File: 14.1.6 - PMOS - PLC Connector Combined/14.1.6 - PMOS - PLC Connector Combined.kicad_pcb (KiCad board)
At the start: 2 copper layers, 61.5 x 67.8 mm, 114 parts, among them J201 Conn_01x01_PAD, J202 Conn_01x01_PAD, J203 Conn_01x01_PAD, J204 Conn_01x01_PAD, J205 Conn_01x01_PAD, J206 Conn_01x01_PAD, J207 Conn_01x01_PAD, J208 Conn_01x01_PAD, J209 Conn_01x01_PAD, J210 Conn_01x01_PAD, J211 Conn_01x01_PAD, J212 Conn_01x01_PAD, J213 Conn_01x01_PAD, J214 Conn_01x01_PAD, J215 Conn_01x01_PAD, J216 Conn_01x01_PAD, J217 Conn_01x01_PAD, J218 Conn_01x01_PAD, J219 Conn_01x01_PAD, J220 Conn_01x01_PAD, J221 DB128L-5.08-2P-BK-S, J222 DB128L-5.08-2P-BK-S, J223 DB128L-5.08-2P-BK-S, J224 DB128L-5.08-2P-BK-S, J225 DB128L-5.08-2P-BK-S, J226 B04B-XASK-1, J301 Conn_01x01_PAD, J302 Conn_01x01_PAD, J303 Conn_01x01_PAD, J304 Conn_01x01_PAD, J305 Conn_01x01_PAD, J306 Conn_01x01_PAD, J307 Conn_01x01_PAD, J308 Conn_01x01_PAD, J309 Conn_01x01_PAD, J310 Conn_01x01_PAD, J311 Conn_01x01_PAD, J312 Conn_01x01_PAD, J313 Conn_01x01_PAD, J314 Conn_01x01_PAD, J315 Conn_01x01_PAD, J316 Conn_01x01_PAD, J317 DB128L-5.08-2P-BK-S, J318 DB128L-5.08-3P-BK-S, J319 DB128L-5.08-2P-BK-S, J320 DB128L-5.08-2P-BK-S, J321 B04B-XASK-1, Q1 2N7002, Q10 DMP6023LE-PMOS, Q2 2N7002, Q3 2N7002, Q4 2N7002, Q5 DMP6023LE-PMOS, Q6 DMP6023LE-PMOS, Q8 DMP6023LE-PMOS

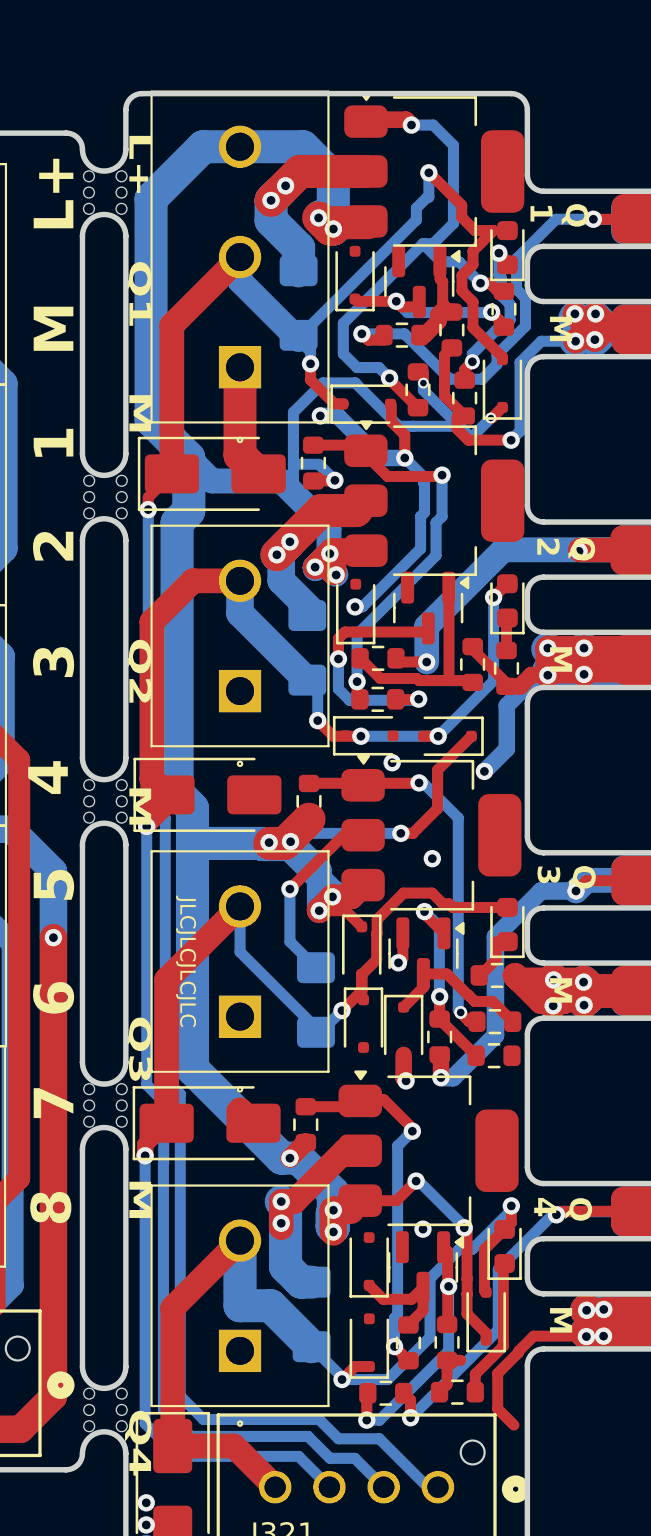
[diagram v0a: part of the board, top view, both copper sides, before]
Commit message: track thickness
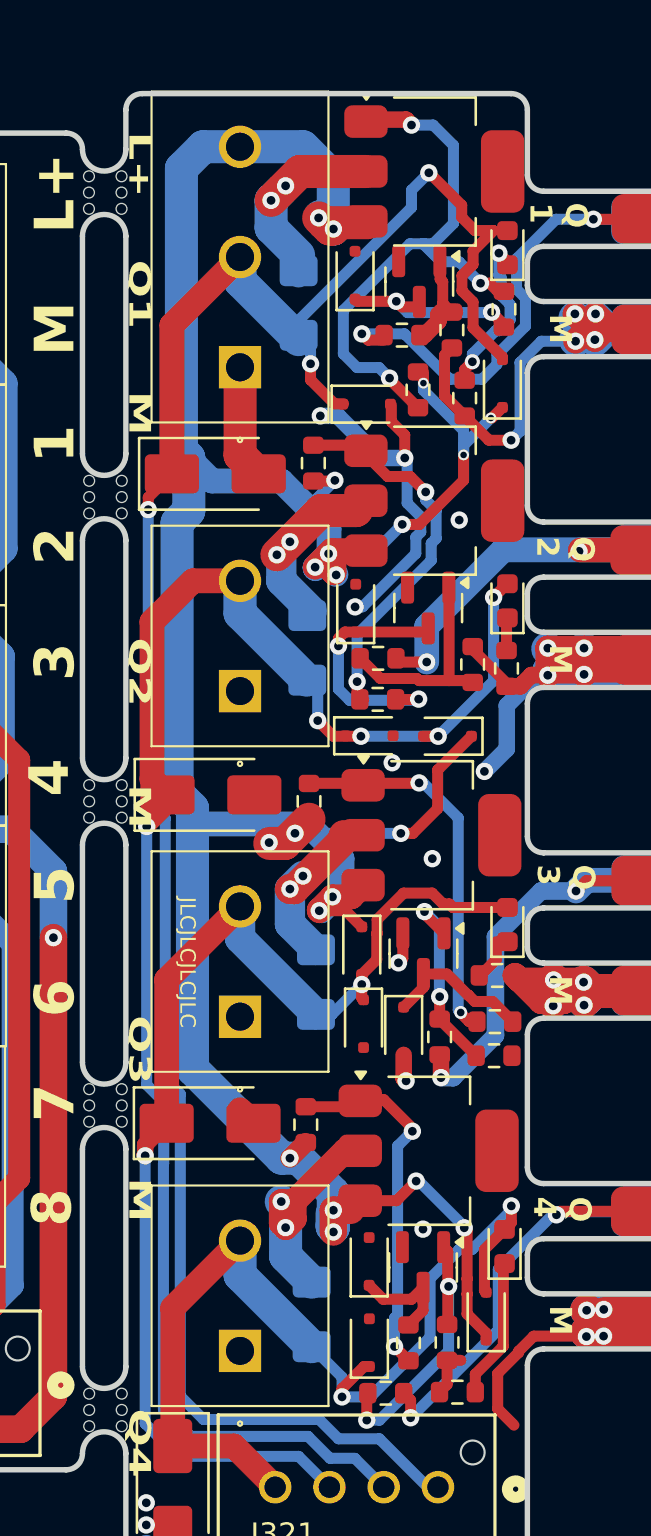
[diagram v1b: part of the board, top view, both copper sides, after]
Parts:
- moved F3 0.83 mm to (111.0, 107.5)
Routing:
- net Net-(D10-K): track 155.8 -> 148.9 mm, vias 18 -> 20
- net Net-(D11-A): track 56.5 -> 55.2 mm
- net Net-(Q6-G): track 18.6 -> 17.5 mm
- net Net-(Q10-D): track 10.9 -> 12.0 mm
- net Net-(D12-K): track 44.3 -> 45.1 mm
- net GNDPWR: track 269.0 -> 268.2 mm, vias 29 -> 30
- net Net-(Q8-D): track 8.95 -> 9.10 mm, vias 1 -> 2
